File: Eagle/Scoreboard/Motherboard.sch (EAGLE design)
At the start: 28 parts

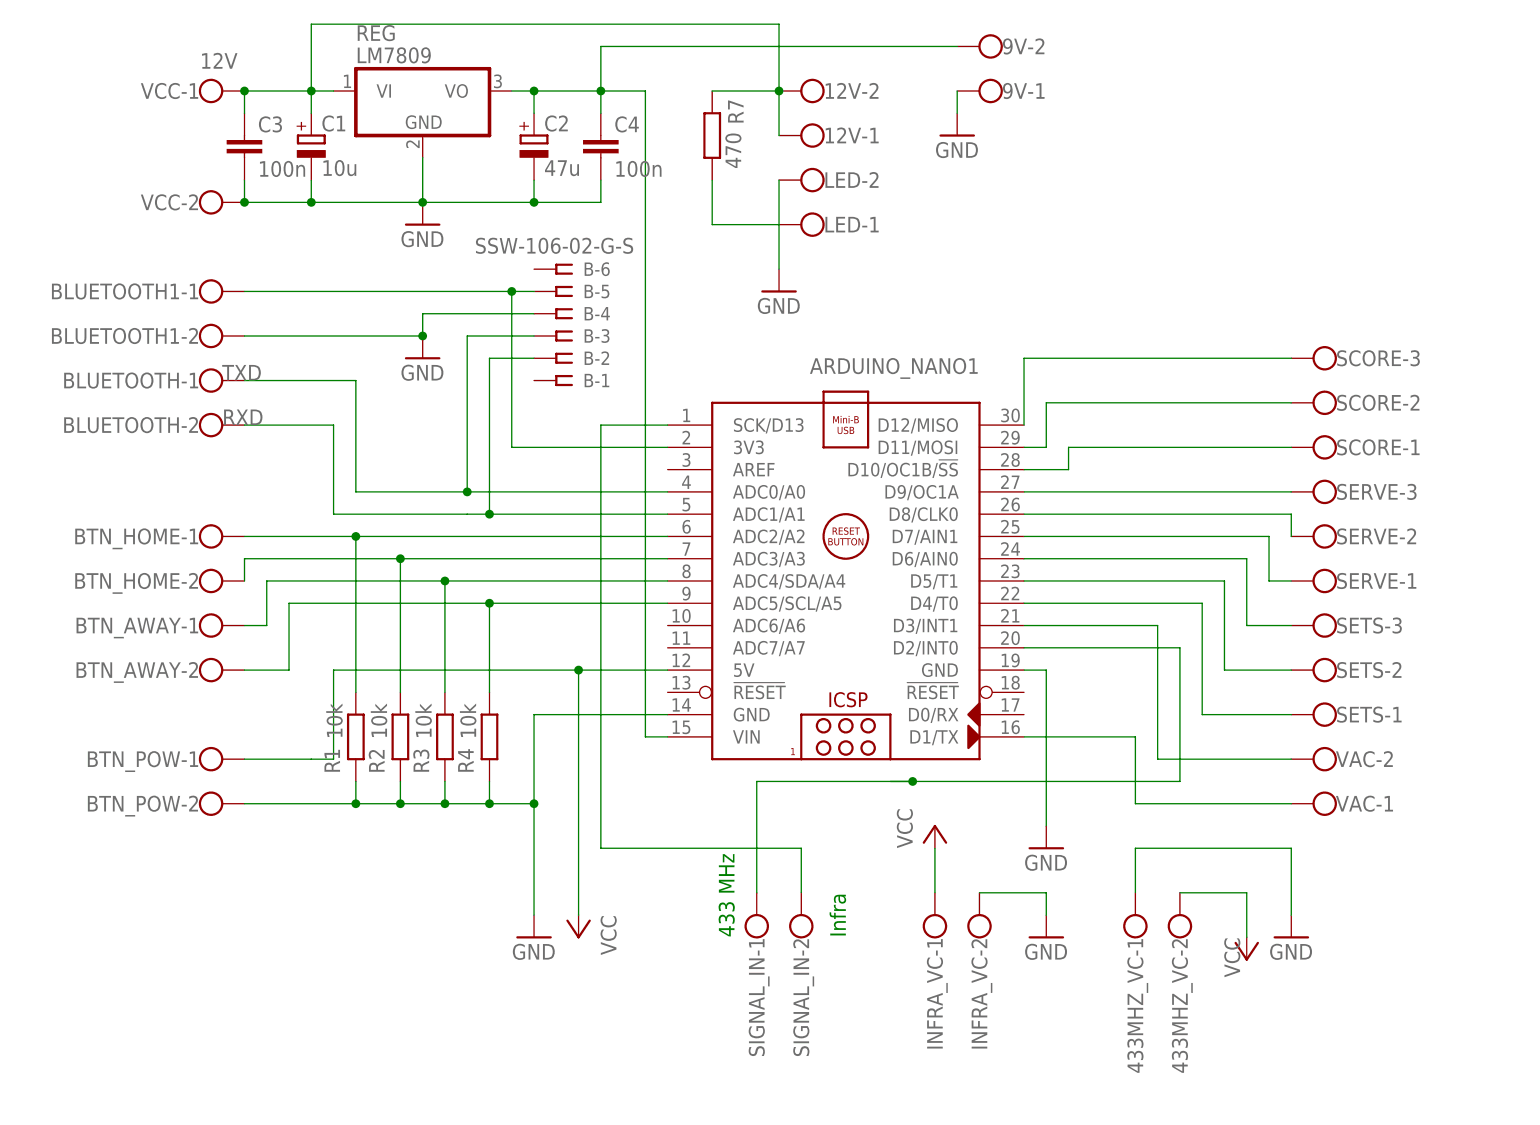
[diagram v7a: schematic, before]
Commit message: Updated schema to reflect latest changes
The 433Mhz pin was moved to A3 and pin A4 and A5 are now used by the real time clock generator
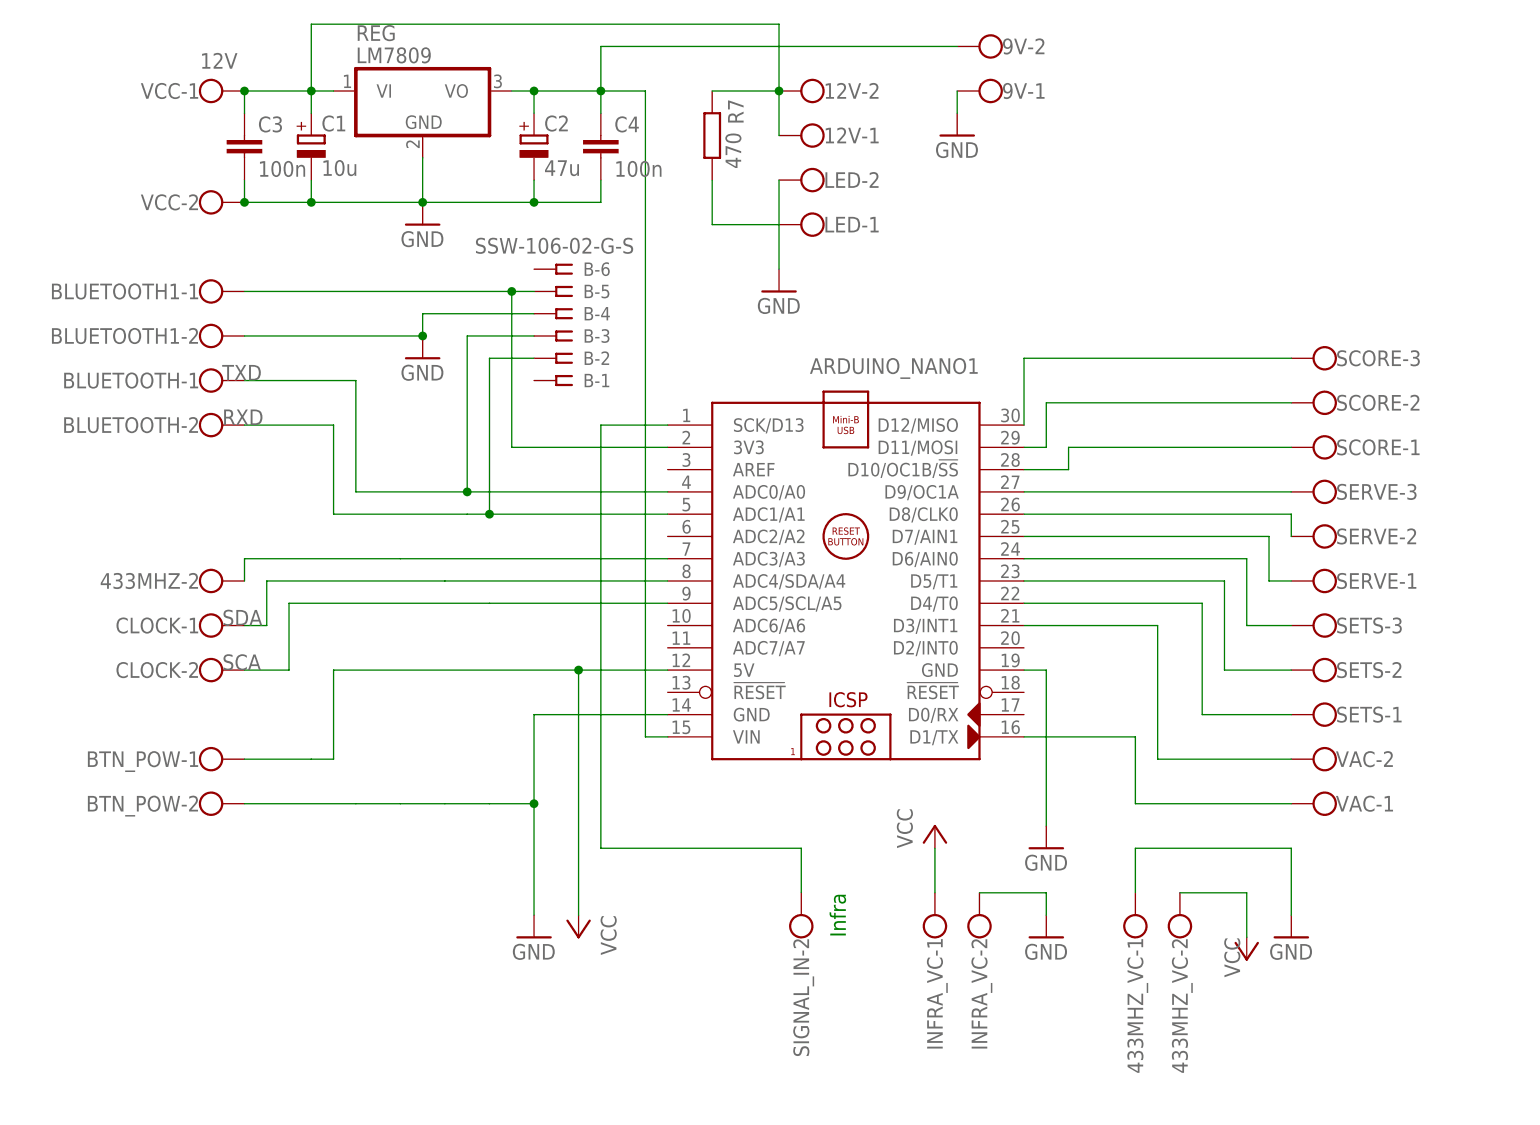
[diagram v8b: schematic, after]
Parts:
- removed BTN_HOME: (no value), con-wago-500:W237-102
- removed R1, R2, R3, R4: 10k, resistor:R-EU_0204/7
- added 433MHZ: (no value), con-wago-500:W237-102
- renumbered BTN_AWAY to CLOCK
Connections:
- removed net A4: ARDUINO_NANO1.ADC4/SDA/A4, CLOCK-1.KL, R3.1
- removed net A5: ARDUINO_NANO1.ADC5/SCL/A5, CLOCK-2.KL, R4.1
- removed net N$1: ARDUINO_NANO1.ADC2/A2, BTN_HOME-1.KL, R1.1
- removed net N$2: ARDUINO_NANO1.ADC3/A3, BTN_HOME-2.KL, R2.1
- new net A4SDA: ARDUINO_NANO1.ADC4/SDA/A4, CLOCK-1.KL
- new net A5SCL: ARDUINO_NANO1.ADC5/SCL/A5, CLOCK-2.KL
- net 433MHZ: now also 433MHZ-2.KL, ARDUINO_NANO1.ADC3/A3; no longer ARDUINO_NANO1.D2/INT0, SIGNAL_IN-1.KL
- net GND: no longer R1.2, R2.2, R3.2, R4.2
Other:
- note added: "SCA"
- note added: "SDA"
- note removed: "433 MHz"
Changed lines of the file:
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@@
 <part name="ARDUINO_NANO1" library="ArduinoNanoV30" deviceset="ARDUINO_NANO" device=""/>
 <part name="REG" library="linear" library_urn="urn:adsk.eagle:library:262" deviceset="78*" device="T" package3d_urn="urn:adsk.eagle:package:16414/1" technology="05" value="LM7809"/>
-<part name="BTN_HOME" library="con-wago-500" library_urn="urn:adsk.eagle:library:195" deviceset="W237-102" device="" package3d_urn="urn:adsk.eagle:package:10688/1"/>
-<part name="BTN_AWAY" library="con-wago-500" library_urn="urn:adsk.eagle:library:195" deviceset="W237-102" device="" package3d_urn="urn:adsk.eagle:package:10688/1"/>
-<part name="R1" library="resistor" library_urn="urn:adsk.eagle:library:348" deviceset="R-EU_" device="0204/7" package3d_urn="urn:adsk.eagle:package:25945/1" value="10k"/>
-<part name="R2" library="resistor" library_urn="urn:adsk.eagle:library:348" deviceset="R-EU_" device="0204/7" package3d_urn="urn:adsk.eagle:package:25945/1" value="10k"/>
-<part name="R3" library="resistor" library_urn="urn:adsk.eagle:library:348" deviceset="R-EU_" device="0204/7" package3d_urn="urn:adsk.eagle:package:25945/1" value="10k"/>
-<part name="R4" library="resistor" library_urn="urn:adsk.eagle:library:348" deviceset="R-EU_" device="0204/7" package3d_urn="urn:adsk.eagle:package:25945/1" value="10k"/>
+<part name="433MHZ" library="con-wago-500" library_urn="urn:adsk.eagle:library:195" deviceset="W237-102" device="" package3d_urn="urn:adsk.eagle:package:10688/1"/>
+<part name="CLOCK" library="con-wago-500" library_urn="urn:adsk.eagle:library:195" deviceset="W237-102" device="" package3d_urn="urn:adsk.eagle:package:10688/1"/>
 <part name="BTN_POW" library="con-wago-500" library_urn="urn:adsk.eagle:library:195" deviceset="W237-102" device="" package3d_urn="urn:adsk.eagle:package:10688/1"/>
 <part name="VCC" library="con-wago-500" library_urn="urn:adsk.eagle:library:195" deviceset="W237-102" device="" package3d_urn="urn:adsk.eagle:package:10688/1"/>
@@
 <text x="-22.86" y="71.12" size="1.778" layer="95">RXD</text>
 <text x="-22.86" y="76.2" size="1.778" layer="95">TXD</text>
-<text x="35.56" y="12.7" size="1.778" layer="91" rot="R90">433 MHz</text>
 <text x="48.26" y="12.7" size="1.778" layer="91" rot="R90">Infra</text>
+<text x="-22.86" y="43.18" size="1.778" layer="95">SCA</text>
+<text x="-22.86" y="48.26" size="1.778" layer="95">SDA</text>
 </plain>
 <instances>
 <instance part="ARDUINO_NANO1" gate="G$1" x="48.26" y="58.42" rot="R180"/>
 <instance part="REG" gate="A1" x="0" y="109.22"/>
-<instance part="BTN_HOME" gate="-1" x="-25.4" y="58.42"/>
-<instance part="BTN_HOME" gate="-2" x="-25.4" y="53.34"/>
-<instance part="BTN_AWAY" gate="-1" x="-25.4" y="48.26"/>
-<instance part="BTN_AWAY" gate="-2" x="-25.4" y="43.18"/>
-<instance part="R1" gate="G$1" x="-7.62" y="35.56" smashed="yes" rot="R270">
-<attribute name="NAME" x="-11.2014" y="34.29" size="1.778" layer="95" rot="R270"/>
-<attribute name="VALUE" x="-10.922" y="39.37" size="1.778" layer="96" rot="R270"/>
-</instance>
-<instance part="R2" gate="G$1" x="-2.54" y="35.56" smashed="yes" rot="R270">
-<attribute name="NAME" x="-6.1214" y="34.29" size="1.778" layer="95" rot="R270"/>
-<attribute name="VALUE" x="-5.842" y="39.37" size="1.778" layer="96" rot="R270"/>
-</instance>
-<instance part="R3" gate="G$1" x="2.54" y="35.56" smashed="yes" rot="R270">
-<attribute name="NAME" x="-1.0414" y="34.29" size="1.778" layer="95" rot="R270"/>
-<attribute name="VALUE" x="-0.762" y="39.37" size="1.778" layer="96" rot="R270"/>
-</instance>
-<instance part="R4" gate="G$1" x="7.62" y="35.56" smashed="yes" rot="R270">
-<attribute name="NAME" x="4.0386" y="34.29" size="1.778" layer="95" rot="R270"/>
-<attribute name="VALUE" x="4.318" y="39.37" size="1.778" layer="96" rot="R270"/>
-</instance>
+<instance part="433MHZ" gate="-2" x="-25.4" y="53.34"/>
+<instance part="CLOCK" gate="-1" x="-25.4" y="48.26"/>
+<instance part="CLOCK" gate="-2" x="-25.4" y="43.18"/>
 <instance part="BTN_POW" gate="-1" x="-25.4" y="33.02"/>
 <instance part="BTN_POW" gate="-2" x="-25.4" y="27.94"/>
@@
 <instance part="LED" gate="-2" x="45.72" y="99.06" rot="R180"/>
 <instance part="GND7" gate="1" x="40.64" y="86.36"/>
-<instance part="SIGNAL_IN" gate="-1" x="38.1" y="12.7" rot="R90"/>
 <instance part="SIGNAL_IN" gate="-2" x="43.18" y="12.7" rot="R90"/>
 <instance part="INFRA_VC" gate="-1" x="58.42" y="12.7" rot="R90"/>
@@
 <wire x1="12.7" y1="27.94" x2="12.7" y2="15.24" width="0.1524" layer="91"/>
 <junction x="12.7" y="27.94"/>
-<pinref part="R4" gate="G$1" pin="2"/>
 <wire x1="7.62" y1="27.94" x2="12.7" y2="27.94" width="0.1524" layer="91"/>
-<wire x1="7.62" y1="30.48" x2="7.62" y2="27.94" width="0.1524" layer="91"/>
-<pinref part="R3" gate="G$1" pin="2"/>
-<wire x1="2.54" y1="30.48" x2="2.54" y2="27.94" width="0.1524" layer="91"/>
 <wire x1="2.54" y1="27.94" x2="7.62" y2="27.94" width="0.1524" layer="91"/>
-<junction x="7.62" y="27.94"/>
-<pinref part="R2" gate="G$1" pin="2"/>
-<wire x1="-2.54" y1="30.48" x2="-2.54" y2="27.94" width="0.1524" layer="91"/>
 <wire x1="-2.54" y1="27.94" x2="2.54" y2="27.94" width="0.1524" layer="91"/>
-<junction x="2.54" y="27.94"/>
-<pinref part="R1" gate="G$1" pin="2"/>
-<wire x1="-7.62" y1="30.48" x2="-7.62" y2="27.94" width="0.1524" layer="91"/>
 <wire x1="-7.62" y1="27.94" x2="-2.54" y2="27.94" width="0.1524" layer="91"/>
-<junction x="-2.54" y="27.94"/>
 <pinref part="BTN_POW" gate="-2" pin="KL"/>
 <wire x1="-20.32" y1="27.94" x2="-7.62" y2="27.94" width="0.1524" layer="91"/>
-<junction x="-7.62" y="27.94"/>
 </segment>
 <segment>
@@
 </segment>
 </net>
-<net name="433MHZ" class="0">
-<segment>
-<wire x1="53.34" y1="30.48" x2="55.88" y2="30.48" width="0.1524" layer="91"/>
-<pinref part="ARDUINO_NANO1" gate="G$1" pin="D2/INT0"/>
-<wire x1="55.88" y1="30.48" x2="86.36" y2="30.48" width="0.1524" layer="91"/>
-<wire x1="68.58" y1="45.72" x2="86.36" y2="45.72" width="0.1524" layer="91"/>
-<wire x1="86.36" y1="45.72" x2="86.36" y2="30.48" width="0.1524" layer="91"/>
-<pinref part="SIGNAL_IN" gate="-1" pin="KL"/>
-<wire x1="55.88" y1="30.48" x2="38.1" y2="30.48" width="0.1524" layer="91"/>
-<wire x1="38.1" y1="30.48" x2="38.1" y2="17.78" width="0.1524" layer="91"/>
-<junction x="55.88" y="30.48"/>
-</segment>
-</net>
 <net name="N$5" class="0">
 <segment>
@@
 </segment>
 </net>
-<net name="N$1" class="0">
-<segment>
-<pinref part="BTN_HOME" gate="-1" pin="KL"/>
-<pinref part="ARDUINO_NANO1" gate="G$1" pin="ADC2/A2"/>
-<wire x1="-20.32" y1="58.42" x2="-7.62" y2="58.42" width="0.1524" layer="91"/>
-<pinref part="R1" gate="G$1" pin="1"/>
-<wire x1="-7.62" y1="58.42" x2="27.94" y2="58.42" width="0.1524" layer="91"/>
-<wire x1="-7.62" y1="40.64" x2="-7.62" y2="58.42" width="0.1524" layer="91"/>
-<junction x="-7.62" y="58.42"/>
-</segment>
-</net>
-<net name="N$2" class="0">
+<net name="433MHZ" class="0">
 <segment>
 <pinref part="ARDUINO_NANO1" gate="G$1" pin="ADC3/A3"/>
-<pinref part="BTN_HOME" gate="-2" pin="KL"/>
+<pinref part="433MHZ" gate="-2" pin="KL"/>
 <wire x1="27.94" y1="55.88" x2="-2.54" y2="55.88" width="0.1524" layer="91"/>
 <wire x1="-2.54" y1="55.88" x2="-20.32" y2="55.88" width="0.1524" layer="91"/>
 <wire x1="-20.32" y1="55.88" x2="-20.32" y2="53.34" width="0.1524" layer="91"/>
-<pinref part="R2" gate="G$1" pin="1"/>
-<wire x1="-2.54" y1="40.64" x2="-2.54" y2="55.88" width="0.1524" layer="91"/>
-<junction x="-2.54" y="55.88"/>
-</segment>
-</net>
-<net name="A4" class="0">
+</segment>
+</net>
+<net name="A4SDA" class="0">
 <segment>
 <pinref part="ARDUINO_NANO1" gate="G$1" pin="ADC4/SDA/A4"/>
@@
 <wire x1="2.54" y1="53.34" x2="-17.78" y2="53.34" width="0.1524" layer="91"/>
 <wire x1="-17.78" y1="53.34" x2="-17.78" y2="48.26" width="0.1524" layer="91"/>
-<pinref part="BTN_AWAY" gate="-1" pin="KL"/>
+<pinref part="CLOCK" gate="-1" pin="KL"/>
 <wire x1="-17.78" y1="48.26" x2="-20.32" y2="48.26" width="0.1524" layer="91"/>
-<pinref part="R3" gate="G$1" pin="1"/>
-<wire x1="2.54" y1="40.64" x2="2.54" y2="53.34" width="0.1524" layer="91"/>
-<junction x="2.54" y="53.34"/>
-</segment>
-</net>
-<net name="A5" class="0">
+</segment>
+</net>
+<net name="A5SCL" class="0">
 <segment>
 <pinref part="ARDUINO_NANO1" gate="G$1" pin="ADC5/SCL/A5"/>
@@
 <wire x1="7.62" y1="50.8" x2="-15.24" y2="50.8" width="0.1524" layer="91"/>
 <wire x1="-15.24" y1="50.8" x2="-15.24" y2="43.18" width="0.1524" layer="91"/>
-<pinref part="BTN_AWAY" gate="-2" pin="KL"/>
+<pinref part="CLOCK" gate="-2" pin="KL"/>
 <wire x1="-15.24" y1="43.18" x2="-20.32" y2="43.18" width="0.1524" layer="91"/>
-<pinref part="R4" gate="G$1" pin="1"/>
-<wire x1="7.62" y1="40.64" x2="7.62" y2="50.8" width="0.1524" layer="91"/>
-<junction x="7.62" y="50.8"/>
-</segment>
-</net>
+</segment>
+</net>
